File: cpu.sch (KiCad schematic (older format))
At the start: 9 parts, among them IC1 STM32L051K8T6, SW1 SW_PUSH

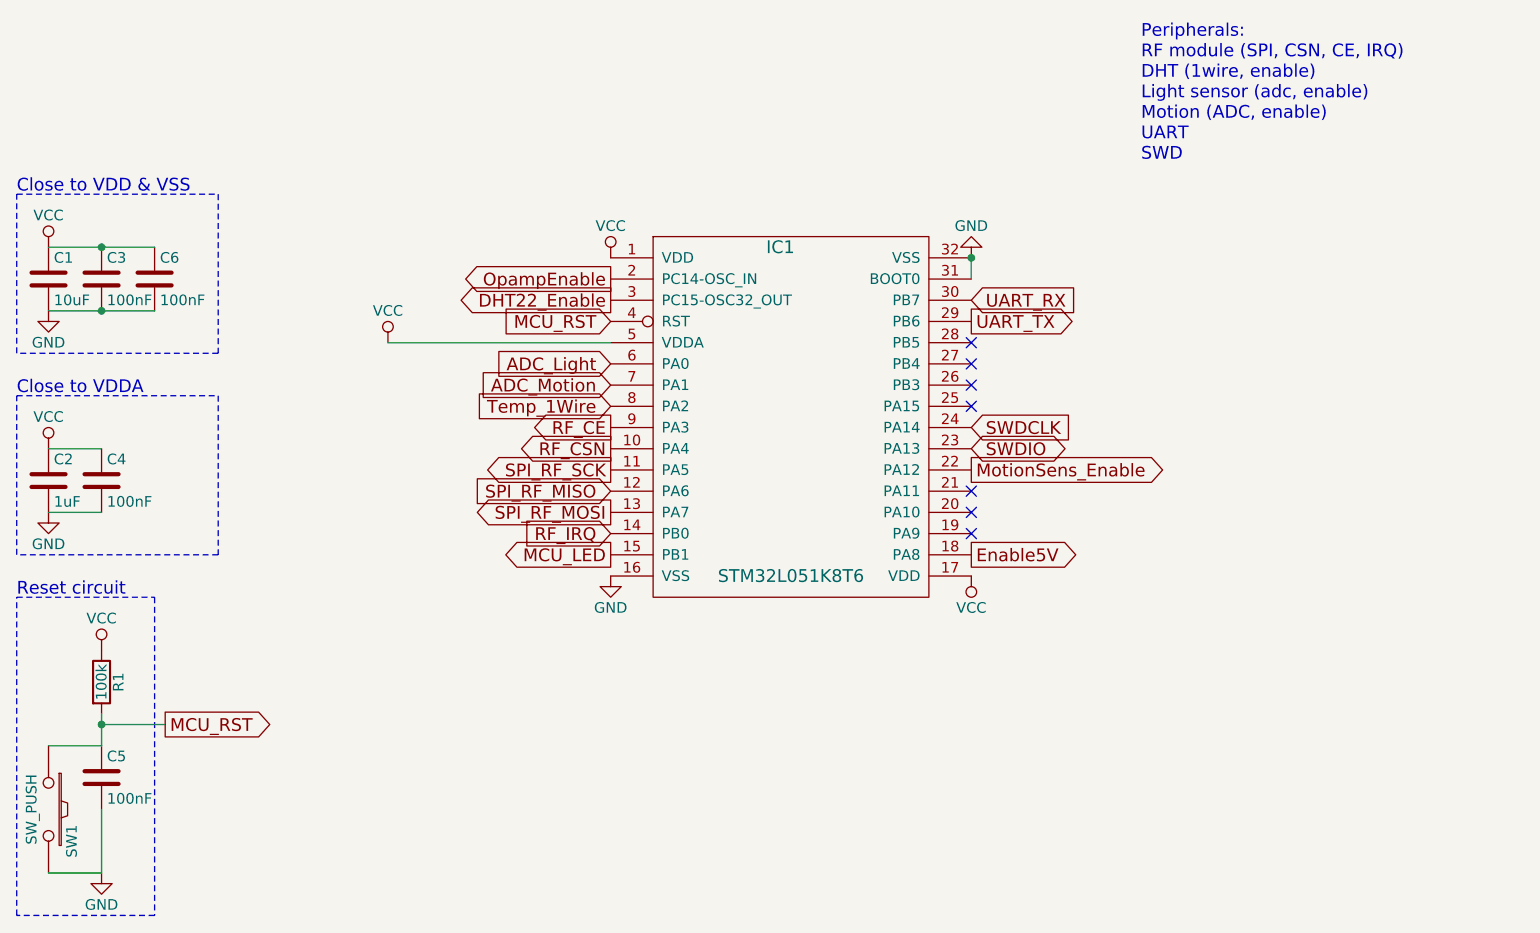
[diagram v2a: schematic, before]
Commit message: Update schematics for V3:
 * Change DHT22 to HTU21D
 * Change schematic for MCP6044
 * Correct unused opamp + power supply
 * Reassign some cpu pins (for HTU21D)
 * Add LDO power supply for 1.8V
 * Update STM32CubeMx project
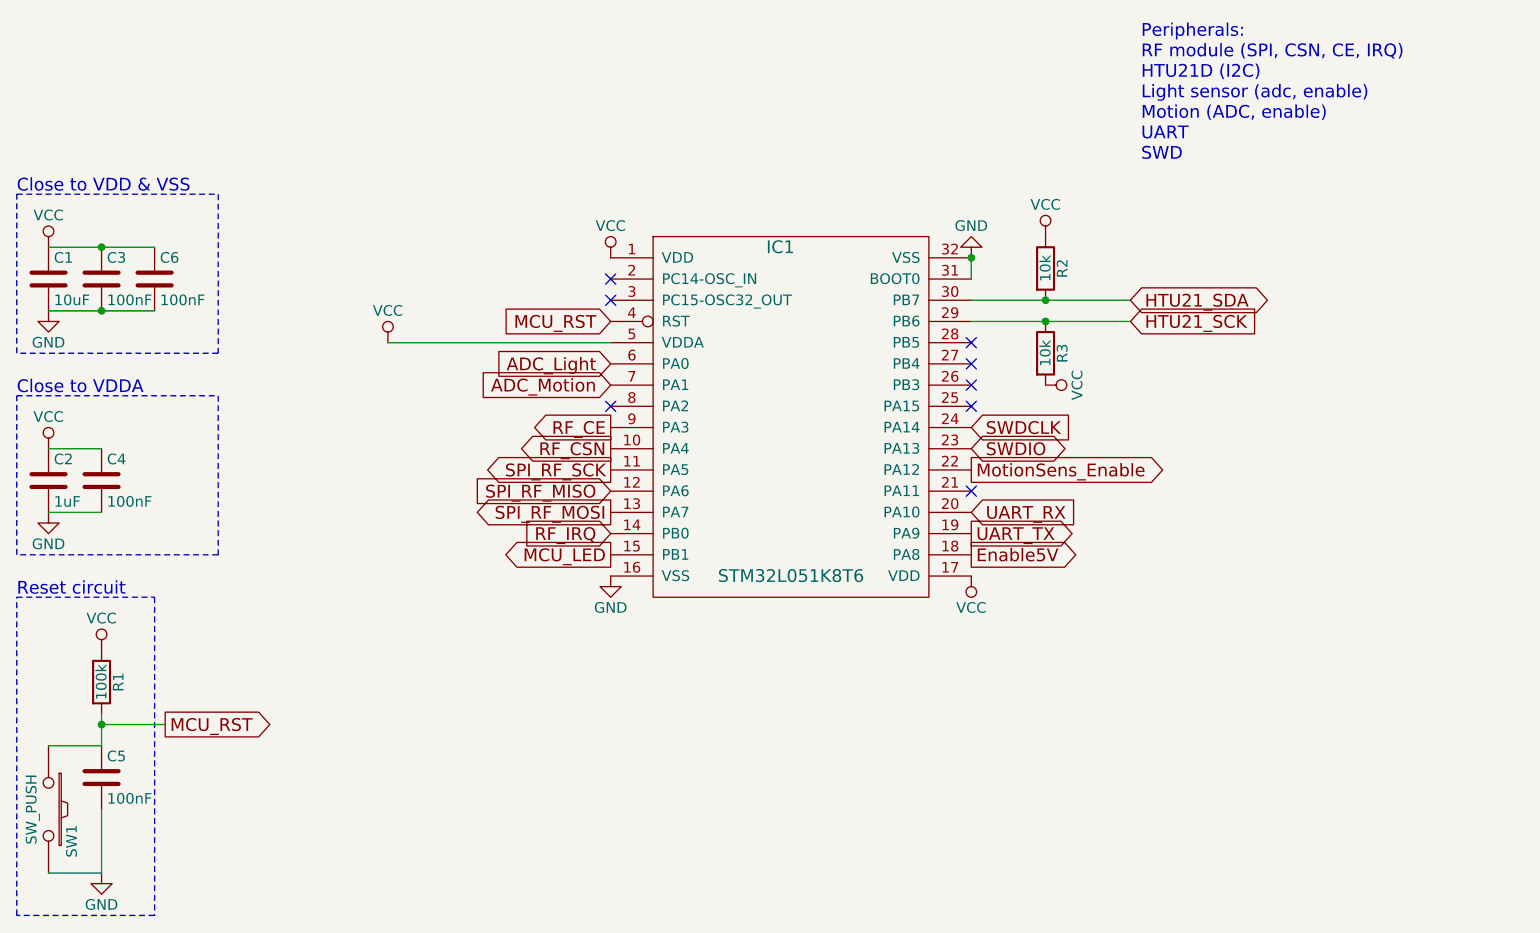
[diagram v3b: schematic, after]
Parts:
- added R2, R3: 10k, symbol R
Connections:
- net UART_RX: now also IC1.20 (PA10); no longer IC1.30 (PB7)
- net UART_TX: now also IC1.19 (PA9); no longer IC1.29 (PB6)
- net VCC: now also R2.1, R3.2
- net DHT22_Enable: no longer names the net of IC1.3 (PC15-OSC32_OUT)
- net OpampEnable: no longer names the net of IC1.2 (PC14-OSC_IN)
- net Temp_1Wire: no longer names the net of IC1.8 (PA2)
- new net HTU21_SCK: IC1.29 (PB6), R3.1
- new net HTU21_SDA: IC1.30 (PB7), R2.2
- no-connect marks 7 -> 8
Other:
- note added: "Peripherals:\nRF module (SPI, CSN, CE, IRQ)\nHTU21D (I2C)\nLight sensor (adc, enable)\nMotion (ADC, enable)\nUART\nSWD"
- note removed: "Peripherals:\nRF module (SPI, CSN, CE, IRQ)\nDHT (1wire, enable)\nLight sensor (adc, enable)\nMotion (ADC, enable)\nUART\nSWD"
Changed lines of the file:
@@
 LIBS:CustomModules
 LIBS:CustomPower
-LIBS:CustomPowerConvertors
 LIBS:CustomTransistors
 LIBS:Custom_ShiftRegisters
@@
 LIBS:Relais
 LIBS:CustomDevices
+LIBS:CustomPowerConvertors
 LIBS:Sensor-cache
 EELAYER 25 0
@@
 $EndDescr
 $Comp
-L VCC #PWR01
+L VCC #PWR1
 U 1 1 565E0F45
 P 2700 3050
-F 0 "#PWR01" H 2700 2900 50  0001 C CNN
+F 0 "#PWR1" H 2700 2900 50  0001 C CNN
 F 1 "VCC" H 2700 3200 50  0000 C CNN
 F 2 "" H 2700 3050 60  0000 C CNN
@@
 $EndComp
 $Comp
-L GND #PWR02
+L GND #PWR2
 U 1 1 565E0F59
 P 2700 3350
-F 0 "#PWR02" H 2700 3100 50  0001 C CNN
+F 0 "#PWR2" H 2700 3100 50  0001 C CNN
 F 1 "GND" H 2700 3200 50  0000 C CNN
 F 2 "" H 2700 3350 60  0000 C CNN
@@
 $EndComp
 $Comp
-L VCC #PWR03
+L VCC #PWR8
 U 1 1 565E1082
 P 5350 3100
-F 0 "#PWR03" H 5350 2950 50  0001 C CNN
+F 0 "#PWR8" H 5350 2950 50  0001 C CNN
 F 1 "VCC" H 5350 3250 50  0000 C CNN
 F 2 "" H 5350 3100 60  0000 C CNN
@@
 $EndComp
 $Comp
-L VCC #PWR04
+L VCC #PWR11
 U 1 1 565E109E
 P 7050 4600
-F 0 "#PWR04" H 7050 4450 50  0001 C CNN
+F 0 "#PWR11" H 7050 4450 50  0001 C CNN
 F 1 "VCC" H 7050 4750 50  0000 C CNN
 F 2 "" H 7050 4600 60  0000 C CNN
@@
 $EndComp
 $Comp
-L GND #PWR05
+L GND #PWR9
 U 1 1 565E10D6
 P 5350 4600
-F 0 "#PWR05" H 5350 4350 50  0001 C CNN
+F 0 "#PWR9" H 5350 4350 50  0001 C CNN
 F 1 "GND" H 5350 4450 50  0000 C CNN
 F 2 "" H 5350 4600 60  0000 C CNN
@@
 $EndComp
 $Comp
-L VCC #PWR06
+L VCC #PWR3
 U 1 1 565E12D0
 P 2700 4000
-F 0 "#PWR06" H 2700 3850 50  0001 C CNN
+F 0 "#PWR3" H 2700 3850 50  0001 C CNN
 F 1 "VCC" H 2700 4150 50  0000 C CNN
 F 2 "" H 2700 4000 60  0000 C CNN
@@
 $EndComp
 $Comp
-L GND #PWR07
+L GND #PWR4
 U 1 1 565E12F0
 P 2700 4300
-F 0 "#PWR07" H 2700 4050 50  0001 C CNN
+F 0 "#PWR4" H 2700 4050 50  0001 C CNN
 F 1 "GND" H 2700 4150 50  0000 C CNN
 F 2 "" H 2700 4300 60  0000 C CNN
@@
 $EndComp
 $Comp
-L VCC #PWR08
+L VCC #PWR5
 U 1 1 565E15CE
 P 2950 4950
-F 0 "#PWR08" H 2950 4800 50  0001 C CNN
+F 0 "#PWR5" H 2950 4800 50  0001 C CNN
 F 1 "VCC" H 2950 5100 50  0000 C CNN
 F 2 "" H 2950 4950 60  0000 C CNN
@@
 $EndComp
 $Comp
-L GND #PWR09
+L GND #PWR6
 U 1 1 565E15F4
 P 2950 6000
-F 0 "#PWR09" H 2950 5750 50  0001 C CNN
+F 0 "#PWR6" H 2950 5750 50  0001 C CNN
 F 1 "GND" H 2950 5850 50  0000 C CNN
 F 2 "" H 2950 6000 60  0000 C CNN
@@
 MCU_RST
 $Comp
-L VCC #PWR010
+L VCC #PWR7
 U 1 1 565E178E
 P 4300 3500
-F 0 "#PWR010" H 4300 3350 50  0001 C CNN
+F 0 "#PWR7" H 4300 3350 50  0001 C CNN
 F 1 "VCC" H 4300 3650 50  0000 C CNN
 F 2 "" H 4300 3500 60  0000 C CNN
@@
 Text GLabel 5350 3700 0    60   Input ~ 0
 ADC_Motion
-Text GLabel 5350 3800 0    60   Input ~ 0
-Temp_1Wire
-Text GLabel 5350 3300 0    60   Output ~ 0
-DHT22_Enable
 Text GLabel 5350 4100 0    60   Output ~ 0
 SPI_RF_SCK
@@
 Text GLabel 7050 4100 2    60   Output ~ 0
 MotionSens_Enable
-Text GLabel 7050 3400 2    60   Output ~ 0
+Text GLabel 7050 4400 2    60   Output ~ 0
 UART_TX
-Text GLabel 7050 3300 2    60   Input ~ 0
+Text GLabel 7050 4300 2    60   Input ~ 0
 UART_RX
-Text GLabel 5350 3200 0    60   Output ~ 0
-OpampEnable
 Text GLabel 7050 4000 2    60   BiDi ~ 0
 SWDIO
@@
 RF_IRQ
 Text Notes 7850 2650 0    60   ~ 0
-Peripherals:\nRF module (SPI, CSN, CE, IRQ)\nDHT (1wire, enable)\nLight sensor (adc, enable)\nMotion (ADC, enable)\nUART\nSWD
+Peripherals:\nRF module (SPI, CSN, CE, IRQ)\nHTU21D (I2C)\nLight sensor (adc, enable)\nMotion (ADC, enable)\nUART\nSWD
 Text GLabel 5350 4500 0    60   Output ~ 0
 MCU_LED
@@
 NoConn ~ 7050 3600
 NoConn ~ 7050 4200
-NoConn ~ 7050 4300
 NoConn ~ 7050 3700
 $Comp
@@
 	1    0    0    -1
 $EndComp
-NoConn ~ 7050 4400
 Text GLabel 7050 4500 2    60   Output ~ 0
 Enable5V
 $Comp
-L GND #PWR011
+L GND #PWR10
 U 1 1 565E10BA
 P 7050 3100
-F 0 "#PWR011" H 7050 2850 50  0001 C CNN
+F 0 "#PWR10" H 7050 2850 50  0001 C CNN
 F 1 "GND" H 7050 2950 50  0000 C CNN
 F 2 "" H 7050 3100 60  0000 C CNN
@@
 Wire Wire Line
 	7050 3100 7050 3200
+NoConn ~ 5350 3300
+NoConn ~ 5350 3800
+Text GLabel 7800 3300 2    60   BiDi ~ 0
+HTU21_SDA
+Text GLabel 7800 3400 2    60   Input ~ 0
+HTU21_SCK
+Wire Wire Line
+	7050 3300 7800 3300
+Wire Wire Line
+	7800 3400 7050 3400
+$Comp
+L R R2
+U 1 1 57536ED2
+P 7400 3150
+F 0 "R2" V 7480 3150 50  0000 C CNN
+F 1 "10k" V 7400 3150 50  0000 C CNN
+F 2 "" V 7330 3150 50  0000 C CNN
+F 3 "" H 7400 3150 50  0000 C CNN
+	1    7400 3150
+	1    0    0    -1
+$EndComp
+Connection ~ 7400 3300
+$Comp
+L VCC #PWR12
+U 1 1 57536F05
+P 7400 3000
+F 0 "#PWR12" H 7400 2850 50  0001 C CNN
+F 1 "VCC" H 7400 3150 50  0000 C CNN
+F 2 "" H 7400 3000 50  0000 C CNN
+F 3 "" H 7400 3000 50  0000 C CNN
+	1    7400 3000
+	1    0    0    -1
+$EndComp
+$Comp
+L R R3
+U 1 1 57536F2D
+P 7400 3550
+F 0 "R3" V 7480 3550 50  0000 C CNN
+F 1 "10k" V 7400 3550 50  0000 C CNN
+F 2 "" V 7330 3550 50  0000 C CNN
+F 3 "" H 7400 3550 50  0000 C CNN
+	1    7400 3550
+	1    0    0    -1
+$EndComp
+$Comp
+L VCC #PWR13
+U 1 1 57536F6A
+P 7400 3700
+F 0 "#PWR13" H 7400 3550 50  0001 C CNN
+F 1 "VCC" H 7400 3850 50  0000 C CNN
+F 2 "" H 7400 3700 50  0000 C CNN
+F 3 "" H 7400 3700 50  0000 C CNN
+	1    7400 3700
+	0    1    1    0
+$EndComp
+Connection ~ 7400 3400
+NoConn ~ 5350 3200
 $EndSCHEMATC

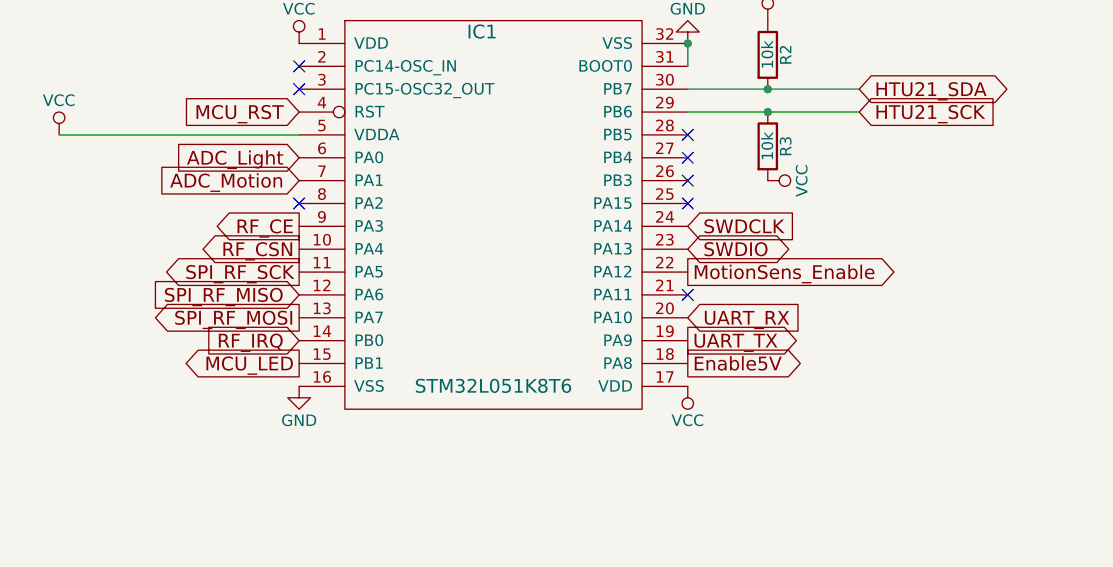
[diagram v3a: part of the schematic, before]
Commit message: Updates for V3:
 * Remove unnecessary power supply enable MOSFETs
 * Optimize pin configuration

Signed-off-by: pluyckx <philip.luyckx@gmail.com>
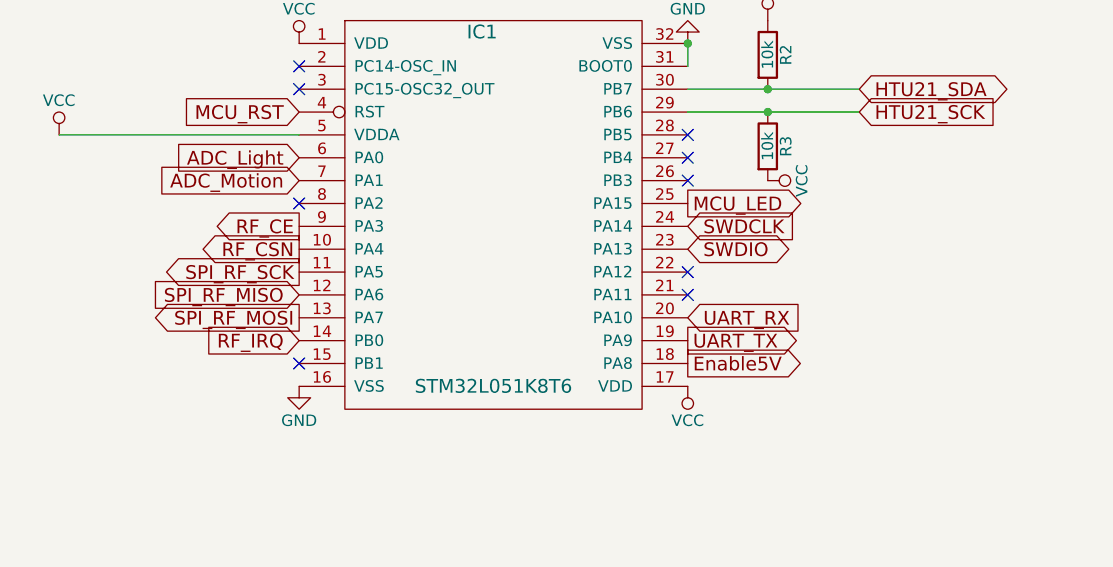
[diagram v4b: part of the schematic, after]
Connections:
- net MCU_LED: now also IC1.25 (PA15); no longer IC1.15 (PB1)
- net MotionSens_Enable: no longer names the net of IC1.22 (PA12)
- no-connect marks 8 -> 9
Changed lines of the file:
@@
 $EndDescr
 $Comp
-L VCC #PWR1
+L VCC #PWR01
 U 1 1 565E0F45
 P 2700 3050
-F 0 "#PWR1" H 2700 2900 50  0001 C CNN
+F 0 "#PWR01" H 2700 2900 50  0001 C CNN
 F 1 "VCC" H 2700 3200 50  0000 C CNN
 F 2 "" H 2700 3050 60  0000 C CNN
@@
 $EndComp
 $Comp
-L GND #PWR2
+L GND #PWR02
 U 1 1 565E0F59
 P 2700 3350
-F 0 "#PWR2" H 2700 3100 50  0001 C CNN
+F 0 "#PWR02" H 2700 3100 50  0001 C CNN
 F 1 "GND" H 2700 3200 50  0000 C CNN
 F 2 "" H 2700 3350 60  0000 C CNN
@@
 $EndComp
 $Comp
-L VCC #PWR8
+L VCC #PWR03
 U 1 1 565E1082
 P 5350 3100
-F 0 "#PWR8" H 5350 2950 50  0001 C CNN
+F 0 "#PWR03" H 5350 2950 50  0001 C CNN
 F 1 "VCC" H 5350 3250 50  0000 C CNN
 F 2 "" H 5350 3100 60  0000 C CNN
@@
 $EndComp
 $Comp
-L VCC #PWR11
+L VCC #PWR04
 U 1 1 565E109E
 P 7050 4600
-F 0 "#PWR11" H 7050 4450 50  0001 C CNN
+F 0 "#PWR04" H 7050 4450 50  0001 C CNN
 F 1 "VCC" H 7050 4750 50  0000 C CNN
 F 2 "" H 7050 4600 60  0000 C CNN
@@
 $EndComp
 $Comp
-L GND #PWR9
+L GND #PWR05
 U 1 1 565E10D6
 P 5350 4600
-F 0 "#PWR9" H 5350 4350 50  0001 C CNN
+F 0 "#PWR05" H 5350 4350 50  0001 C CNN
 F 1 "GND" H 5350 4450 50  0000 C CNN
 F 2 "" H 5350 4600 60  0000 C CNN
@@
 $EndComp
 $Comp
-L VCC #PWR3
+L VCC #PWR06
 U 1 1 565E12D0
 P 2700 4000
-F 0 "#PWR3" H 2700 3850 50  0001 C CNN
+F 0 "#PWR06" H 2700 3850 50  0001 C CNN
 F 1 "VCC" H 2700 4150 50  0000 C CNN
 F 2 "" H 2700 4000 60  0000 C CNN
@@
 $EndComp
 $Comp
-L GND #PWR4
+L GND #PWR07
 U 1 1 565E12F0
 P 2700 4300
-F 0 "#PWR4" H 2700 4050 50  0001 C CNN
+F 0 "#PWR07" H 2700 4050 50  0001 C CNN
 F 1 "GND" H 2700 4150 50  0000 C CNN
 F 2 "" H 2700 4300 60  0000 C CNN
@@
 $EndComp
 $Comp
-L VCC #PWR5
+L VCC #PWR08
 U 1 1 565E15CE
 P 2950 4950
-F 0 "#PWR5" H 2950 4800 50  0001 C CNN
+F 0 "#PWR08" H 2950 4800 50  0001 C CNN
 F 1 "VCC" H 2950 5100 50  0000 C CNN
 F 2 "" H 2950 4950 60  0000 C CNN
@@
 $EndComp
 $Comp
-L GND #PWR6
+L GND #PWR09
 U 1 1 565E15F4
 P 2950 6000
-F 0 "#PWR6" H 2950 5750 50  0001 C CNN
+F 0 "#PWR09" H 2950 5750 50  0001 C CNN
 F 1 "GND" H 2950 5850 50  0000 C CNN
 F 2 "" H 2950 6000 60  0000 C CNN
@@
 MCU_RST
 $Comp
-L VCC #PWR7
+L VCC #PWR010
 U 1 1 565E178E
 P 4300 3500
-F 0 "#PWR7" H 4300 3350 50  0001 C CNN
+F 0 "#PWR010" H 4300 3350 50  0001 C CNN
 F 1 "VCC" H 4300 3650 50  0000 C CNN
 F 2 "" H 4300 3500 60  0000 C CNN
@@
 Text GLabel 5350 4300 0    60   Output ~ 0
 SPI_RF_MOSI
-Text GLabel 7050 4100 2    60   Output ~ 0
-MotionSens_Enable
 Text GLabel 7050 4400 2    60   Output ~ 0
 UART_TX
@@
 Text Notes 7850 2650 0    60   ~ 0
 Peripherals:\nRF module (SPI, CSN, CE, IRQ)\nHTU21D (I2C)\nLight sensor (adc, enable)\nMotion (ADC, enable)\nUART\nSWD
-Text GLabel 5350 4500 0    60   Output ~ 0
+Text GLabel 7050 3800 2    60   Output ~ 0
 MCU_LED
-NoConn ~ 7050 3800
+NoConn ~ 5350 4500
 NoConn ~ 7050 3500
 NoConn ~ 7050 3600
@@
 Enable5V
 $Comp
-L GND #PWR10
+L GND #PWR011
 U 1 1 565E10BA
 P 7050 3100
-F 0 "#PWR10" H 7050 2850 50  0001 C CNN
+F 0 "#PWR011" H 7050 2850 50  0001 C CNN
 F 1 "GND" H 7050 2950 50  0000 C CNN
 F 2 "" H 7050 3100 60  0000 C CNN
@@
 Connection ~ 7400 3300
 $Comp
-L VCC #PWR12
+L VCC #PWR012
 U 1 1 57536F05
 P 7400 3000
-F 0 "#PWR12" H 7400 2850 50  0001 C CNN
+F 0 "#PWR012" H 7400 2850 50  0001 C CNN
 F 1 "VCC" H 7400 3150 50  0000 C CNN
 F 2 "" H 7400 3000 50  0000 C CNN
@@
 $EndComp
 $Comp
-L VCC #PWR13
+L VCC #PWR013
 U 1 1 57536F6A
 P 7400 3700
-F 0 "#PWR13" H 7400 3550 50  0001 C CNN
+F 0 "#PWR013" H 7400 3550 50  0001 C CNN
 F 1 "VCC" H 7400 3850 50  0000 C CNN
 F 2 "" H 7400 3700 50  0000 C CNN
@@
 Connection ~ 7400 3400
 NoConn ~ 5350 3200
+NoConn ~ 7050 4100
 $EndSCHEMATC

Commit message: Finish schematic, assign all footprints for V3
Signed-off-by: pluyckx <philip.luyckx@gmail.com>
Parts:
- R2, R3: footprint (none) -> Resistors_SMD:R_0603
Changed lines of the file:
@@
 encoding utf-8
 Sheet 2 6
-Title ""
-Date ""
-Rev ""
-Comp ""
+Title "Sensor"
+Date "2016-06-05"
+Rev "3"
+Comp "Philip Luyckx"
 Comment1 ""
 Comment2 ""
@@
 F 0 "R2" V 7480 3150 50  0000 C CNN
 F 1 "10k" V 7400 3150 50  0000 C CNN
-F 2 "" V 7330 3150 50  0000 C CNN
+F 2 "Resistors_SMD:R_0603" V 7330 3150 50  0001 C CNN
 F 3 "" H 7400 3150 50  0000 C CNN
 	1    7400 3150
@@
 F 0 "R3" V 7480 3550 50  0000 C CNN
 F 1 "10k" V 7400 3550 50  0000 C CNN
-F 2 "" V 7330 3550 50  0000 C CNN
+F 2 "Resistors_SMD:R_0603" V 7330 3550 50  0001 C CNN
 F 3 "" H 7400 3550 50  0000 C CNN
 	1    7400 3550

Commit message: Update some routing
Signed-off-by: pluyckx <philip.luyckx@gmail.com>
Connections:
- net ADC_Light: now also IC1.7 (PA1); no longer IC1.6 (PA0)
- net ADC_Motion: now also IC1.8 (PA2); no longer IC1.7 (PA1)
- new net DIG_Motion: IC1.6 (PA0)
- no-connect marks 9 -> 8
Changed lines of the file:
@@
 Text Notes 2550 4700 0    60   ~ 0
 Reset circuit
-Text GLabel 5350 3600 0    60   Input ~ 0
+Text GLabel 5350 3700 0    60   Input ~ 0
 ADC_Light
-Text GLabel 5350 3700 0    60   Input ~ 0
+Text GLabel 5350 3800 0    60   Input ~ 0
 ADC_Motion
 Text GLabel 5350 4100 0    60   Output ~ 0
@@
 	7050 3100 7050 3200
 NoConn ~ 5350 3300
-NoConn ~ 5350 3800
 Text GLabel 7800 3300 2    60   BiDi ~ 0
 HTU21_SDA
@@
 NoConn ~ 5350 3200
 NoConn ~ 7050 4100
+Text GLabel 5350 3600 0    60   Input ~ 0
+DIG_Motion
 $EndSCHEMATC
